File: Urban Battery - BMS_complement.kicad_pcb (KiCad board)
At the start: 2 copper layers, 149.9 x 83.8 mm, 37 parts, among them J1 BMS IO, J10 Thermistor, J11 Thermistor, J12 CAN Connector, J13 CAN Connector, J2 OLED Header, J3 E-Stop, J4 E-Stop, J5 E-Stop, J6 Contactor Connector, J7 Charge Connector, J8 Battery Connector, J9 Thermistor, K1 Contactor_Relay, K2 Charge_Relay, SW1 SW_Push_LED, SW2 SW_DPDT_x2, SW3 CAN_TERM, U1 MCP2515-xSO, U2 LM2575HVS-12/NOPB, U3 MCP2551-I-SN, Y1 8MHz

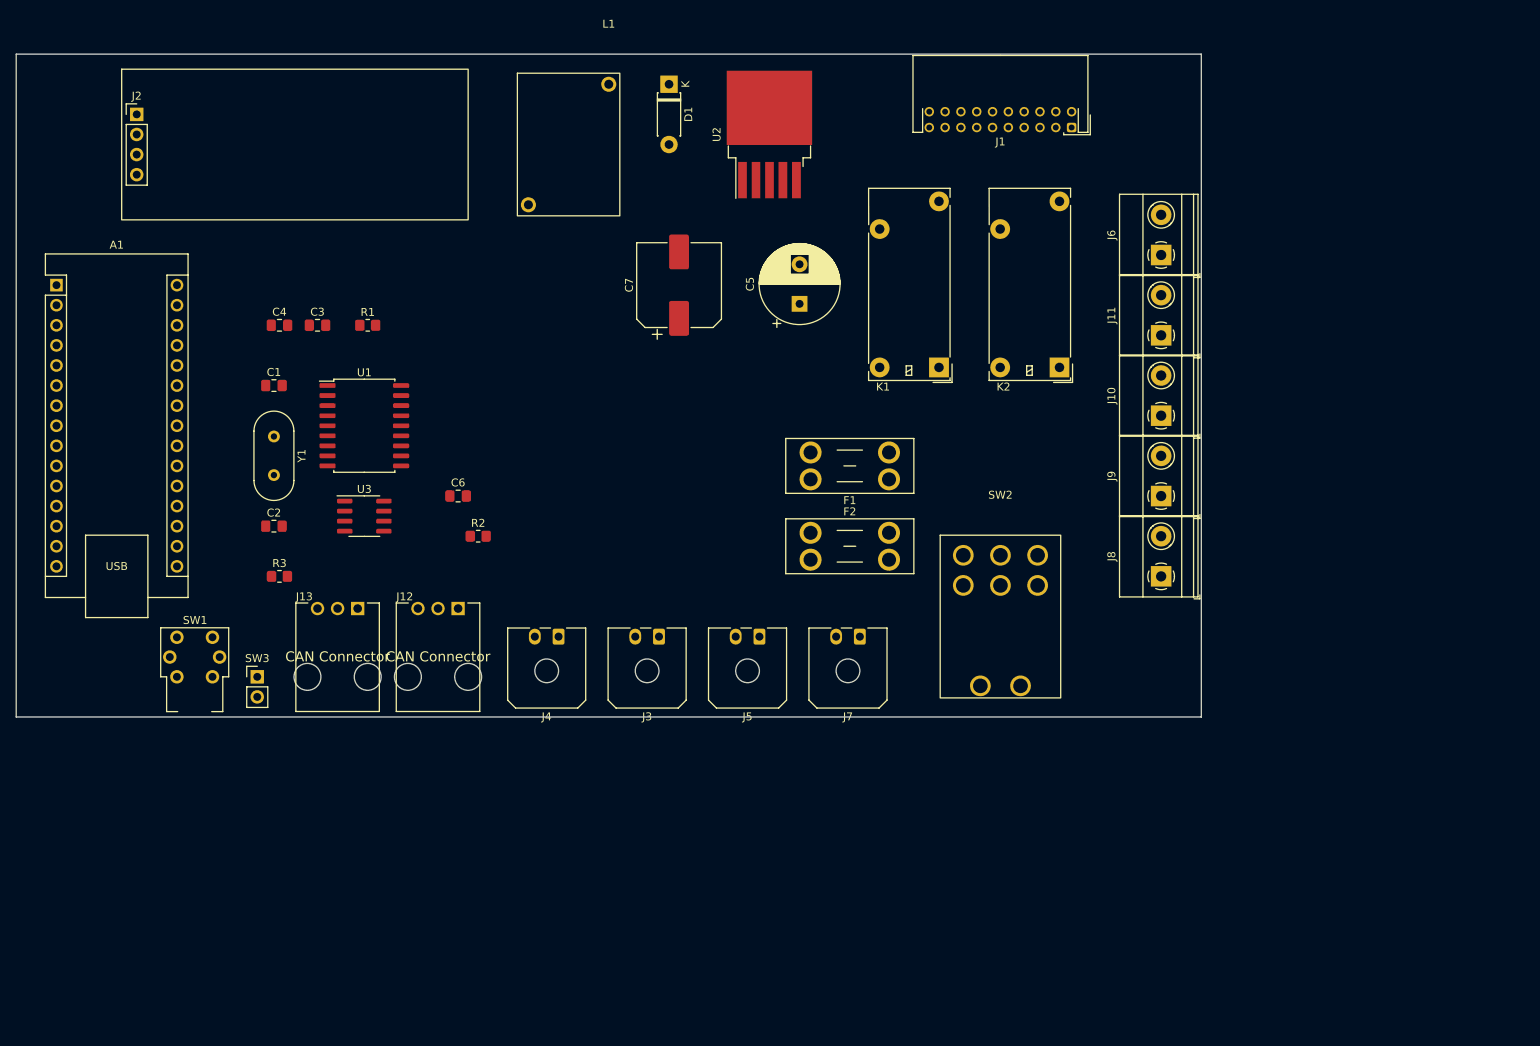
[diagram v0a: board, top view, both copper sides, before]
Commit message: Edited component placement
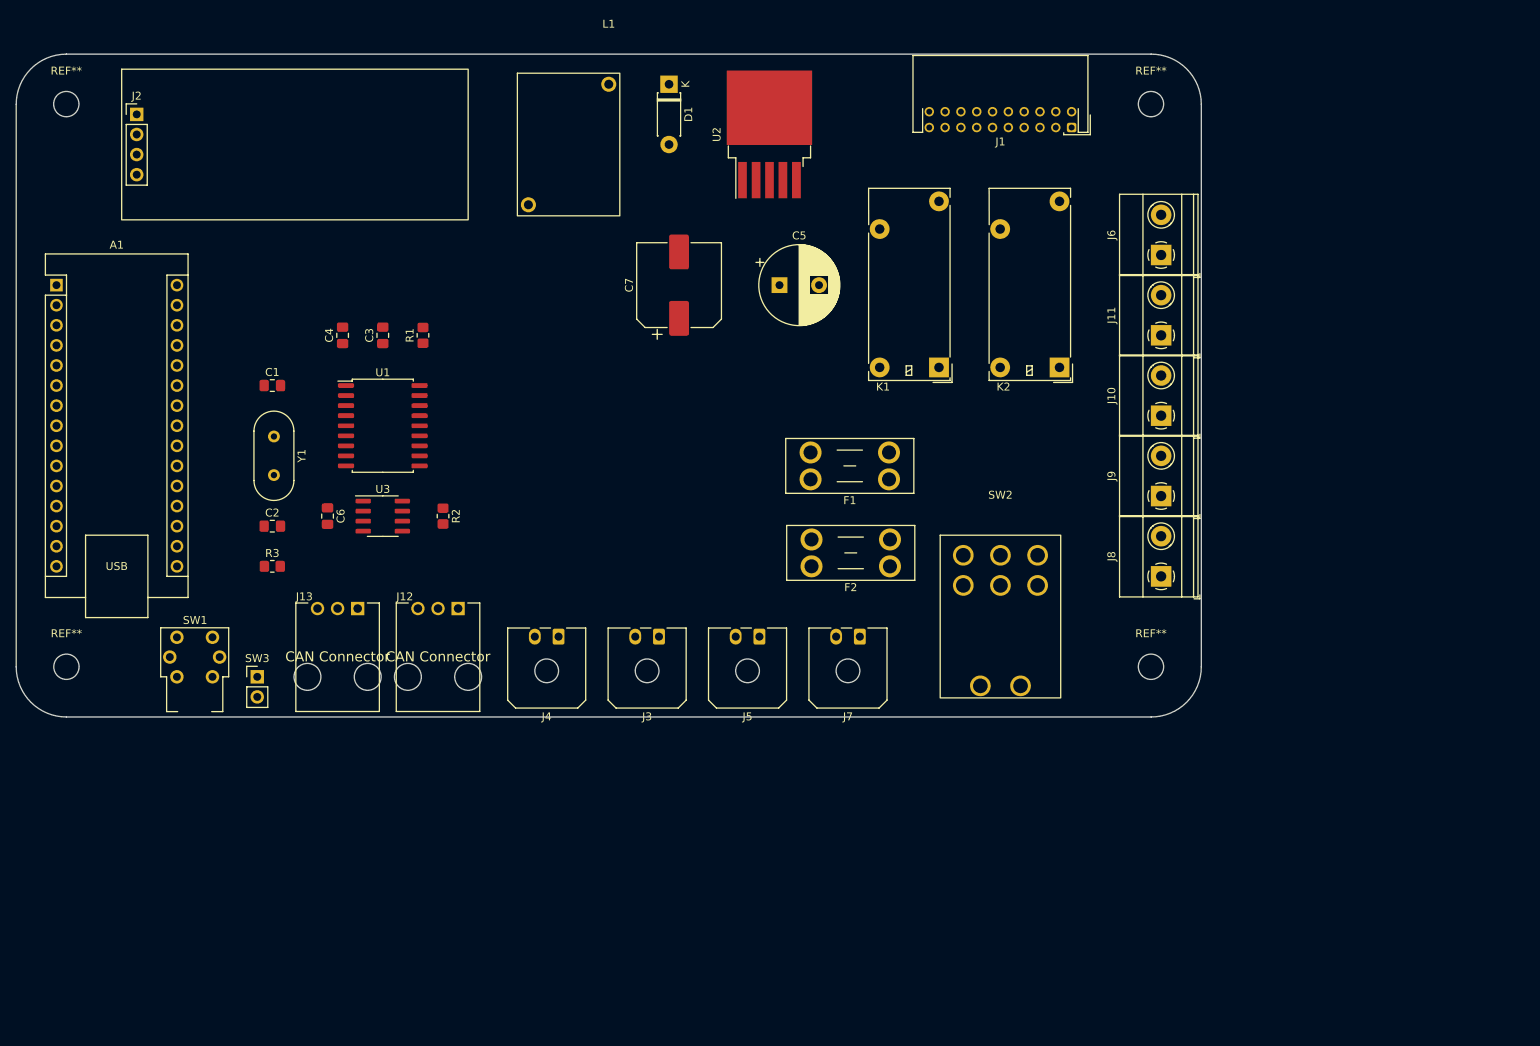
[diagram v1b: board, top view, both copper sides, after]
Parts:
- added REF**: MountingHole_3.2mm_M3, MountingHole:MountingHole_3.2mm_M3, F.Cu at (219.7, 128.3)
- added REF**: MountingHole_3.2mm_M3, MountingHole:MountingHole_3.2mm_M3, F.Cu at (219.7, 57.1)
- added REF**: MountingHole_3.2mm_M3, MountingHole:MountingHole_3.2mm_M3, F.Cu at (82.5, 57.1)
- added REF**: MountingHole_3.2mm_M3, MountingHole:MountingHole_3.2mm_M3, F.Cu at (82.5, 128.3)
- moved C6 16.7 mm to (115.6, 109.2), turned to -90 degrees
- moved F2 10.9 mm to (186.7, 115.6), turned to 180 degrees
- moved C3 8.35 mm to (122.6, 86.4), turned to 90 degrees
- moved C4 8.09 mm to (117.5, 86.4), turned to 90 degrees
- moved R1 7.10 mm to (127.6, 86.4), turned to 90 degrees
- moved R2 5.12 mm to (130.2, 109.2), turned to -90 degrees
- moved C5 3.47 mm to (172.7, 80.0), turned to 0 degrees
- moved U1 2.34 mm to (122.6, 97.8)
- moved U3 2.34 mm to (122.6, 109.2)
- moved R3 1.56 mm to (108.6, 115.6)
- moved C1 0.21 mm to (108.6, 92.7)
- moved C2 0.21 mm to (108.6, 110.5)
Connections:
- net Net-(C1-Pad2) renamed C+
- net Net-(C2-Pad2) renamed C-
- C3 pad 1: GND -> +5V
- C3 pad 2: +5V -> GND
- R1 pad 1: Net-(R1-Pad1) -> +5V
- R1 pad 2: +5V -> Net-(U1-Pad17)
- U1 pad 17: Net-(R1-Pad1) -> Net-(U1-Pad17)
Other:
- outline, holes or cut-outs redrawn

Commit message: reorganized layout, started routing traces and added supermileage logo
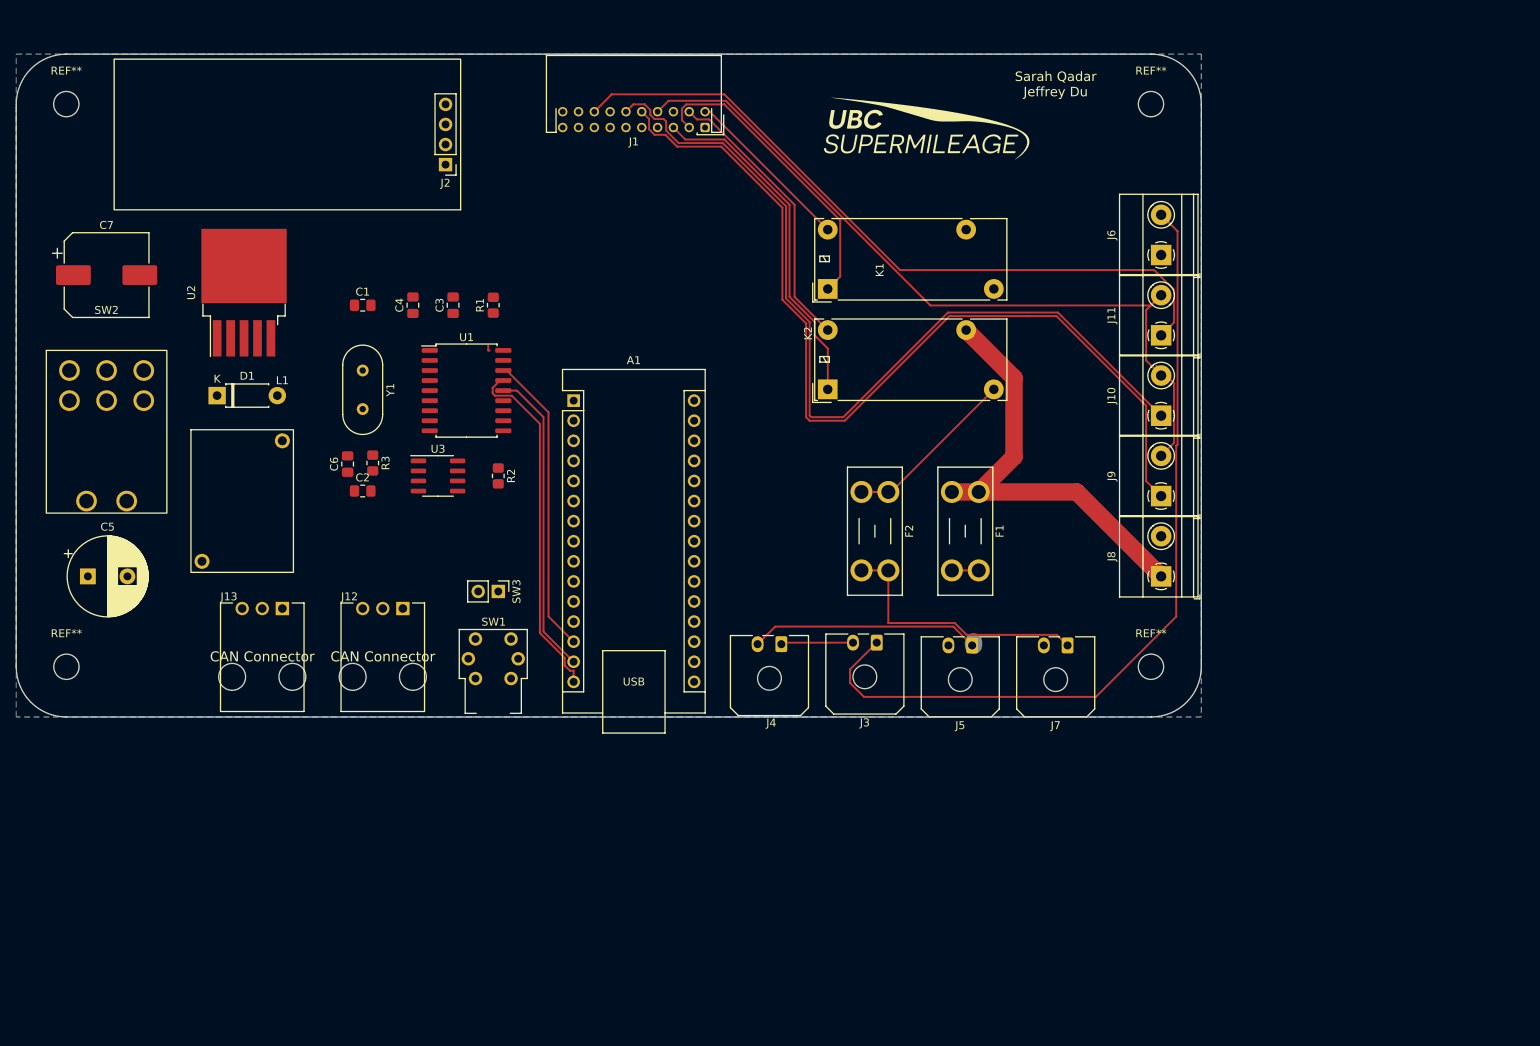
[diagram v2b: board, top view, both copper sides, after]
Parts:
- added G***: LOGO, LOGO, F.Cu at (191.1, 61.0)
- moved SW2 115.4 mm to (87.6, 90.8)
- moved C5 94.9 mm to (85.3, 116.8)
- moved C7 72.4 mm to (87.6, 78.7), turned to 0 degrees
- moved D1 69.4 mm to (101.6, 94.0), turned to 0 degrees
- moved U2 69.4 mm to (105.0, 81.0)
- moved A1 67.0 mm to (146.7, 94.6)
- moved L1 61.1 mm to (109.9, 99.7)
- moved J1 46.4 mm to (163.3, 60.1)
- moved J2 39.6 mm to (130.5, 64.8), turned to 180 degrees
- moved SW1 37.8 mm to (134.3, 129.8)
- moved SW3 32.3 mm to (137.2, 118.7), turned to -90 degrees
- moved K2 29.4 mm to (178.8, 93.2), turned to 90 degrees
- moved J4 28.2 mm to (172.9, 125.4)
- moved J3 27.5 mm to (185.0, 125.2)
- moved J5 26.9 mm to (197.1, 125.6)
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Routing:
- net bms10: track 0.00 -> 117.6 mm
- net bms12: track 0.00 -> 110.1 mm
- net Net-(J3-Pad1): track 0.00 -> 104.4 mm
- net bms8: track 0.00 -> 100.3 mm
- net bms16: track 0.00 -> 90.9 mm
- net +48V: track 0.00 -> 55.7 mm
- net MISO: track 0.00 -> 44.7 mm
- net bms5: track 0.00 -> 44.1 mm
- net MOSI: track 0.00 -> 39.0 mm
- net bms3: track 0.00 -> 38.4 mm
- net CAN_CS: track 0.00 -> 38.2 mm
- net bms4: track 0.00 -> 35.8 mm
- net Net-(F2-Pad2): track 0.00 -> 33.9 mm
- net Net-(J4-Pad2): track 0.00 -> 29.5 mm
- net Net-(F2-Pad1): track 0.00 -> 22.1 mm
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- added copper zone on B.Cu, net GND
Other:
- board text added: "Sarah Qadar Jeffrey Du"

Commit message: updated layout from schematic, deleted traces
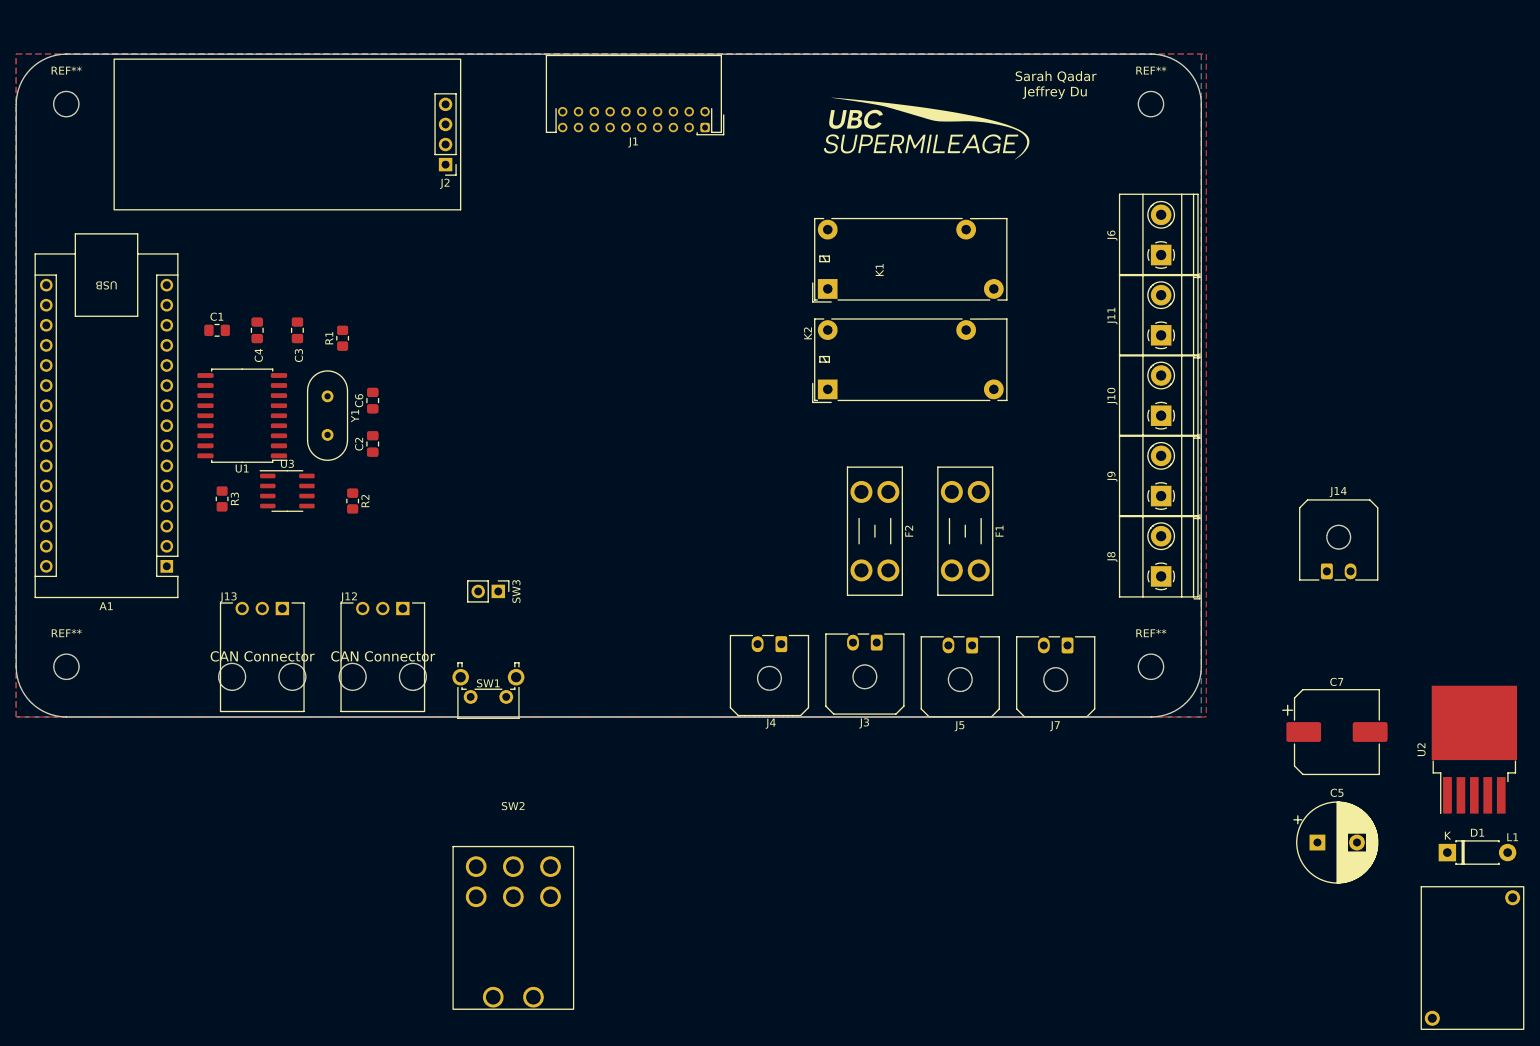
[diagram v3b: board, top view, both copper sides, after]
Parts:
- added J14: E-Stop, Connector_Molex:Molex_Micro-Fit_3.0_43650-0200_1x02_P3.00mm_Horizontal, F.Cu at (241.9, 116.2)
- SW1: value SW_Push_LED -> SW_SPST; footprint Button_Switch_THT:SW_Push_1P1T_NO_LED_E-Switch_TL1250 -> Button_Switch_THT:SW_Tactile_SPST_Angled_PTS645Vx31-2LFS
- moved C7 166.0 mm to (243.2, 136.5)
- moved D1 166.0 mm to (257.2, 151.8)
- moved L1 166.0 mm to (265.4, 157.5)
- moved U2 166.0 mm to (260.6, 138.7)
- moved C5 159.1 mm to (240.7, 150.5)
- moved SW2 81.1 mm to (139.1, 153.5)
- moved A1 55.5 mm to (95.2, 115.6), turned to 180 degrees
- moved U1 28.5 mm to (104.8, 96.5), turned to 180 degrees
- moved C3 19.9 mm to (111.8, 85.7)
- moved C4 19.9 mm to (106.7, 85.7)
- moved R3 19.6 mm to (102.2, 107.0)
- moved R1 19.5 mm to (117.5, 86.7)
- moved U3 19.1 mm to (110.5, 106.0)
- moved C1 18.7 mm to (101.6, 85.7)
- moved R2 18.7 mm to (118.7, 107.3)
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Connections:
- A1 pad 12: unconnected-(A1-Pad12) -> CAN_INT
- A1 pad 8: unconnected-(A1-Pad8) -> Net-(A1-Pad8)
- J2 pad 3: Net-(J2-Pad3) -> +5V
- J5 pad 1: Net-(J4-Pad2) -> Net-(J5-Pad1)
- SW1 pad 1: Net-(J2-Pad3) -> GND
- SW1 pad 2: +5V -> Net-(A1-Pad8)
- U1 pad 12: unconnected-(U1-Pad12) -> CAN_INT
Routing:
- net bms10: track 117.6 -> 0.00 mm
- net bms12: track 110.1 -> 0.00 mm
- net Net-(J3-Pad1): track 104.4 -> 0.00 mm
- net bms8: track 100.3 -> 0.00 mm
- net bms16: track 90.9 -> 0.00 mm
- net +48V: track 55.7 -> 0.00 mm
- net MISO: track 44.7 -> 0.00 mm
- net bms5: track 44.1 -> 0.00 mm
- net MOSI: track 39.0 -> 0.00 mm
- net bms3: track 38.4 -> 0.00 mm
- net CAN_CS: track 38.2 -> 0.00 mm
- net bms4: track 35.8 -> 0.00 mm
- net Net-(F2-Pad2): track 33.9 -> 0.00 mm
- net Net-(J4-Pad2): track 29.5 -> 0.00 mm
- net Net-(F2-Pad1): track 22.1 -> 0.00 mm
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- added copper zone on F.Cu, net +5V
